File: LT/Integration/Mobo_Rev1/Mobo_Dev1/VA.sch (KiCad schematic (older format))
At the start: 27 parts, among them J2 Conn_Coaxial, J3 Conn_01x02_Male, J4 Conn_01x02_Male, U1 BAP64Q

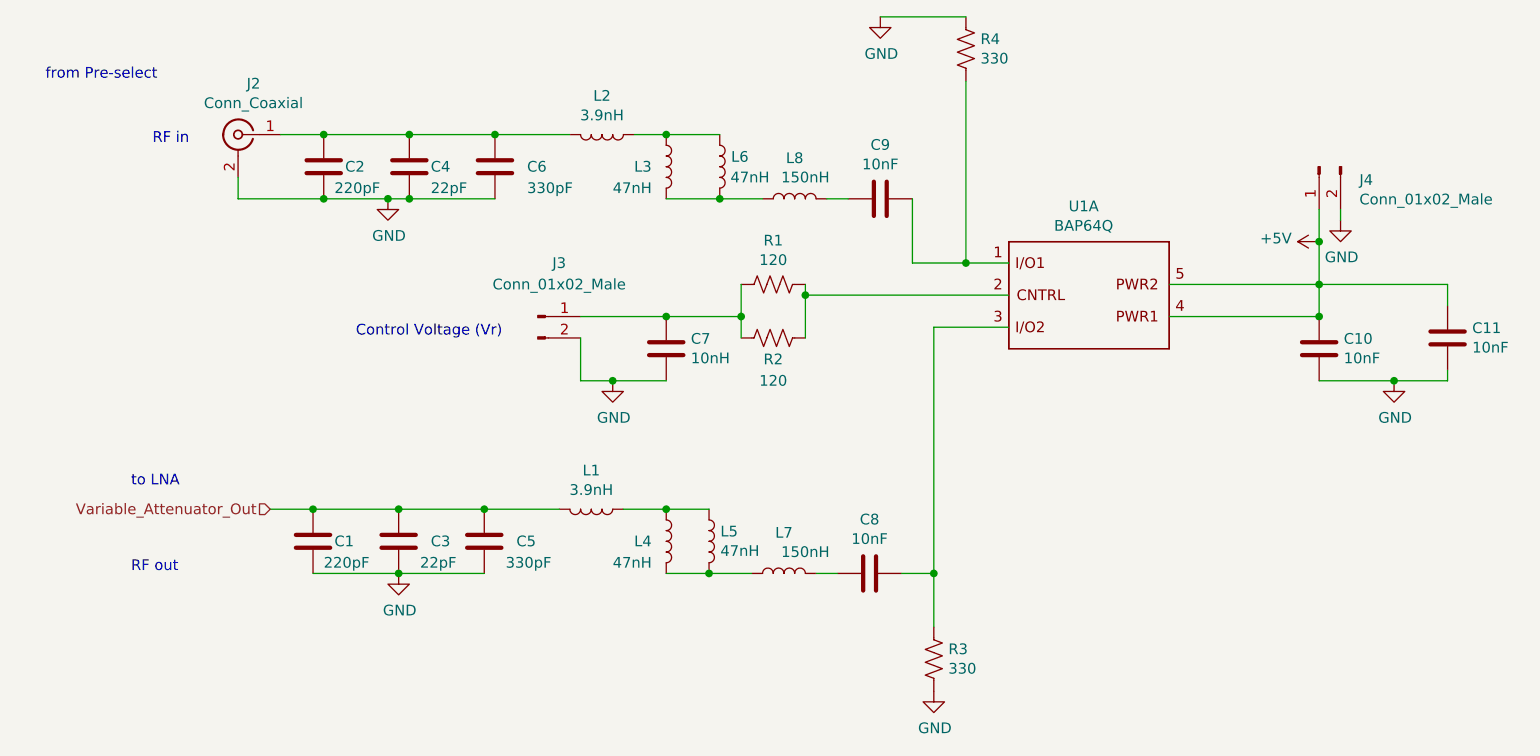
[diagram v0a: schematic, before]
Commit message: Added the preliminary layout for the Phase 2 motherboard, not at all finished yet
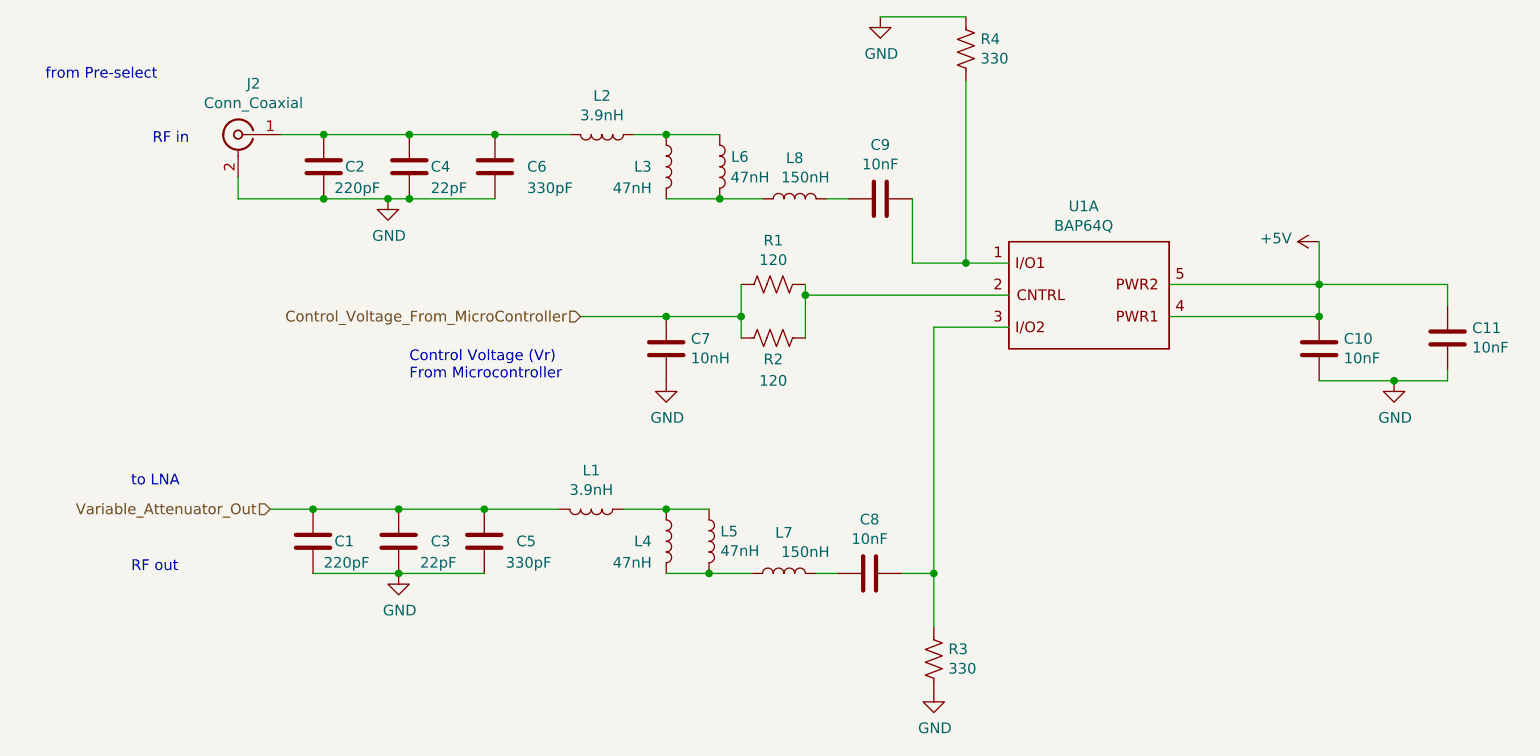
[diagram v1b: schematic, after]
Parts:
- removed J3, J4: Conn_01x02_Male, Connector_PinHeader_2.54mm:PinHeader_1x02_P2.54mm_Vertical, symbol Connector:Conn_01x02_Male
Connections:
- net Control_Voltage_From_MicroController: now reaches C7.1, R1.2, R2.2
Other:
- note added: "Control Voltage (Vr)\nFrom Microcontroller"
- note removed: "Control Voltage (Vr)"
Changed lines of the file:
@@
 Wire Wire Line
 	5550 3250 5550 3350
-$Comp
-L Connector:Conn_01x02_Male J3
-U 1 1 5E4F0CB6
-P 4600 3250
-F 0 "J3" H 4700 3500 50  0000 C CNN
-F 1 "Conn_01x02_Male" H 4700 3400 50  0000 C CNN
-F 2 "Connector_PinHeader_2.54mm:PinHeader_1x02_P2.54mm_Vertical" H 4600 3250 50  0001 C CNN
-F 3 "~" H 4600 3250 50  0001 C CNN
-	1    4600 3250
-	1    0    0    -1
-$EndComp
-Wire Wire Line
-	4800 3250 5200 3250
-Connection ~ 5200 3250
-Wire Wire Line
-	4800 3350 4800 3550
-Wire Wire Line
-	4800 3550 4950 3550
 Wire Wire Line
 	5850 3150 6800 3150
@@
 	0    -1   -1   0
 $EndComp
-Connection ~ 8250 2900
-Wire Wire Line
-	8250 2900 8250 2750
-$Comp
-L Connector:Conn_01x02_Male J4
-U 1 1 5E50C337
-P 8250 2550
-F 0 "J4" V 8312 2362 50  0000 R CNN
-F 1 "Conn_01x02_Male" V 8403 2362 50  0000 R CNN
-F 2 "Connector_PinHeader_2.54mm:PinHeader_1x02_P2.54mm_Vertical" H 8250 2550 50  0001 C CNN
-F 3 "~" H 8250 2550 50  0001 C CNN
-	1    8250 2550
-	0    -1   1    0
-$EndComp
 Wire Wire Line
 	8250 3550 8600 3550
@@
 	3900 2700 4000 2700
 $Comp
-L power:GND #PWR03
-U 1 1 5E529B3F
-P 4950 3550
-F 0 "#PWR03" H 4950 3300 50  0001 C CNN
-F 1 "GND" H 4955 3377 50  0000 C CNN
-F 2 "" H 4950 3550 50  0001 C CNN
-F 3 "" H 4950 3550 50  0001 C CNN
-	1    4950 3550
-	1    0    0    -1
-$EndComp
-Connection ~ 4950 3550
-Wire Wire Line
-	4950 3550 5200 3550
-$Comp
 L power:GND #PWR08
 U 1 1 5E529E75
@@
 	8600 3550 8850 3550
 $Comp
-L power:GND #PWR07
-U 1 1 5E52A360
-P 8350 2800
-F 0 "#PWR07" H 8350 2550 50  0001 C CNN
-F 1 "GND" H 8355 2627 50  0000 C CNN
-F 2 "" H 8350 2800 50  0001 C CNN
-F 3 "" H 8350 2800 50  0001 C CNN
-	1    8350 2800
-	1    0    0    -1
-$EndComp
-$Comp
 L power:GND #PWR04
 U 1 1 5E52A954
@@
 	1    0    0    -1
 $EndComp
-Wire Wire Line
-	8350 2750 8350 2800
-Text Notes 3750 3350 0    50   ~ 0
-Control Voltage (Vr)
 Text Notes 2300 2150 0    50   ~ 0
 from Pre-select
@@
 Text HLabel 3350 4150 0    50   Input ~ 0
 Variable_Attenuator_Out
+$Comp
+L power:GND #PWR03
+U 1 1 5E529B3F
+P 5200 3550
+F 0 "#PWR03" H 5200 3300 50  0001 C CNN
+F 1 "GND" H 5205 3377 50  0000 C CNN
+F 2 "" H 5200 3550 50  0001 C CNN
+F 3 "" H 5200 3550 50  0001 C CNN
+	1    5200 3550
+	1    0    0    -1
+$EndComp
+Connection ~ 5200 3250
+Wire Wire Line
+	4800 3250 5200 3250
+Text Notes 4000 3550 0    50   ~ 0
+Control Voltage (Vr)\nFrom Microcontroller
+Text HLabel 4800 3250 0    50   Input ~ 0
+Control_Voltage_From_MicroController
 $EndSCHEMATC
